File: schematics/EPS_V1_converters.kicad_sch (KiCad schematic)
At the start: 30 parts, among them U2 TPS62132RGTR, U3 TPS62133RGTR, U6 TPS61088RHLR

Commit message: Fix NC pins, add 2 test points & silkscreen labels
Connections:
- net GND: now also U2.4 (PG), U3.4 (PG), U6.11 (NC), U6.12 (NC)
- no-connect marks 5 -> 1
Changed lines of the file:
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@@
 	)
 	(junction
+		(at 135.89 166.37)
+		(diameter 0)
+		(color 0 0 0 0)
+	)
+	(junction
 		(at 137.16 134.62)
 		(diameter 0)
@@
 	)
 	(junction
+		(at 69.85 95.25)
+		(diameter 0)
+		(color 0 0 0 0)
+	)
+	(junction
 		(at 59.69 156.21)
 		(diameter 0)
@@
 	)
 	(junction
+		(at 134.62 127)
+		(diameter 0)
+		(color 0 0 0 0)
+	)
+	(junction
 		(at 114.3 54.61)
 		(diameter 0)
@@
 	)
 	(junction
-		(at 129.54 171.45)
+		(at 134.62 124.46)
 		(diameter 0)
 		(color 0 0 0 0)
 	)
 	(junction
-		(at 105.41 67.31)
+		(at 129.54 171.45)
 		(diameter 0)
 		(color 0 0 0 0)
 	)
 	(junction
-		(at 134.62 124.46)
+		(at 105.41 67.31)
 		(diameter 0)
 		(color 0 0 0 0)
@@
 	)
 	(junction
-		(at 135.89 163.83)
-		(diameter 0)
-		(color 0 0 0 0)
-	)
-	(junction
 		(at 114.3 57.15)
 		(diameter 0)
@@
 	)
 	(junction
+		(at 135.89 163.83)
+		(diameter 0)
+		(color 0 0 0 0)
+	)
+	(junction
 		(at 114.3 49.53)
 		(diameter 0)
@@
 		(at 69.85 85.09)
 	)
-	(no_connect
-		(at 129.54 166.37)
-	)
-	(no_connect
-		(at 69.85 95.25)
-	)
-	(no_connect
-		(at 129.54 127)
-	)
-	(no_connect
-		(at 69.85 92.71)
-	)
 	(wire
 		(pts
@@
 	(wire
 		(pts
+			(xy 135.89 166.37) (xy 135.89 163.83)
+		)
+		(stroke
+			(width 0)
+			(type default)
+		)
+	)
+	(wire
+		(pts
 			(xy 45.72 64.77) (xy 69.85 64.77)
 		)
@@
 	(wire
 		(pts
-			(xy 134.62 124.46) (xy 134.62 125.73)
+			(xy 134.62 124.46) (xy 134.62 127)
 		)
 		(stroke
@@
 	(wire
 		(pts
+			(xy 129.54 166.37) (xy 135.89 166.37)
+		)
+		(stroke
+			(width 0)
+			(type default)
+		)
+	)
+	(wire
+		(pts
 			(xy 45.72 156.21) (xy 59.69 156.21)
 		)
@@
 	(wire
 		(pts
+			(xy 69.85 92.71) (xy 69.85 95.25)
+		)
+		(stroke
+			(width 0)
+			(type default)
+		)
+	)
+	(wire
+		(pts
 			(xy 68.58 41.91) (xy 69.85 41.91)
 		)
@@
 	(wire
 		(pts
+			(xy 129.54 127) (xy 134.62 127)
+		)
+		(stroke
+			(width 0)
+			(type default)
+		)
+	)
+	(wire
+		(pts
 			(xy 105.41 29.21) (xy 114.3 29.21)
 		)
@@
 	(symbol
 		(lib_id "power:GND")
-		(at 135.89 163.83 0)
+		(at 135.89 166.37 0)
 		(unit 1)
 		(body_style 1)
@@
 		(dnp no)
 		(property "Reference" "#PWR017"
-			(at 135.89 170.18 0)
+			(at 135.89 172.72 0)
 			(hide yes)
 			(show_name no)
@@
 		)
 		(property "Value" "GND"
-			(at 135.89 167.894 0)
+			(at 135.89 170.434 0)
 			(show_name no)
 			(do_not_autoplace no)
@@
 		)
 		(property "Footprint" ""
-			(at 135.89 163.83 0)
+			(at 135.89 166.37 0)
 			(hide yes)
 			(show_name no)
@@
 		)
 		(property "Datasheet" ""
-			(at 135.89 163.83 0)
+			(at 135.89 166.37 0)
 			(hide yes)
 			(show_name no)
@@
 		)
 		(property "Description" "Power symbol creates a global label with name \"GND\" , ground"
-			(at 135.89 163.83 0)
+			(at 135.89 166.37 0)
 			(hide yes)
 			(show_name no)
@@
 	(symbol
 		(lib_id "power:GND")
-		(at 134.62 125.73 0)
+		(at 134.62 127 0)
 		(unit 1)
 		(body_style 1)
@@
 		(dnp no)
 		(property "Reference" "#PWR023"
-			(at 134.62 132.08 0)
+			(at 134.62 133.35 0)
 			(hide yes)
 			(show_name no)
@@
 		)
 		(property "Value" "GND"
-			(at 134.62 129.794 0)
+			(at 134.62 131.064 0)
 			(show_name no)
 			(do_not_autoplace no)
@@
 		)
 		(property "Footprint" ""
-			(at 134.62 125.73 0)
+			(at 134.62 127 0)
 			(hide yes)
 			(show_name no)
@@
 		)
 		(property "Datasheet" ""
-			(at 134.62 125.73 0)
+			(at 134.62 127 0)
 			(hide yes)
 			(show_name no)
@@
 		)
 		(property "Description" "Power symbol creates a global label with name \"GND\" , ground"
-			(at 134.62 125.73 0)
+			(at 134.62 127 0)
 			(hide yes)
 			(show_name no)
@@
 					(unit 1)
 				)
+			)
+		)
+	)
+	(symbol
+		(lib_id "power:GND")
+		(at 69.85 95.25 0)
+		(unit 1)
+		(body_style 1)
+		(exclude_from_sim no)
+		(in_bom yes)
+		(on_board yes)
+		(in_pos_files yes)
+		(dnp no)
+		(property "Reference" "#PWR081"
+			(at 69.85 101.6 0)
+			(hide yes)
+			(show_name no)
+			(do_not_autoplace no)
+			(effects
+				(font
+					(size 1.27 1.27)
+				)
+			)
+		)
+		(property "Value" "GND"
+			(at 69.85 99.314 0)
+			(show_name no)
+			(do_not_autoplace no)
+			(effects
+				(font
+					(size 1.27 1.27)
+				)
+			)
+		)
+		(property "Footprint" ""
+			(at 69.85 95.25 0)
+			(hide yes)
+			(show_name no)
+			(do_not_autoplace no)
+			(effects
+				(font
+					(size 1.27 1.27)
+				)
+			)
+		)
+		(property "Datasheet" ""
+			(at 69.85 95.25 0)
+			(hide yes)
+			(show_name no)
+			(do_not_autoplace no)
+			(effects
+				(font
+					(size 1.27 1.27)
+				)
+			)
+		)
+		(property "Description" "Power symbol creates a global label with name \"GND\" , ground"
+			(at 69.85 95.25 0)
+			(hide yes)
+			(show_name no)
+			(do_not_autoplace no)
+			(effects
+				(font
+					(size 1.27 1.27)
+				)
+			)
+		)
+		(pin "1"
+		)
+		(instances
+			(project "EPS_V1"
+				(path "/85157432-5d03-48fa-ab40-27ed3d133f47/d39b1cbe-de60-4da6-b23b-bfd89ef5271a"
+					(reference "#PWR081")
+					(unit 1)
+				)

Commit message: Fix silkscreen; Fix component value style
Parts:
- C2, C6, C_AVIN1, C_AVIN2: value 0.1u -> 100n
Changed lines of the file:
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@@
 			)
 		)
-		(property "Value" "0.1u"
+		(property "Value" "100n"
 			(at 42.926 133.35 0)
 			(show_name no)
@@
 			)
 		)
-		(property "Value" "0.1u"
+		(property "Value" "100n"
 			(at 108.204 39.37 0)
 			(show_name no)
@@
 			)
 		)
-		(property "Value" "0.1u"
+		(property "Value" "100n"
 			(at 49.276 44.45 0)
 			(show_name no)
@@
 			)
 		)
-		(property "Value" "0.1u"
+		(property "Value" "100n"
 			(at 42.926 172.72 0)
 			(show_name no)

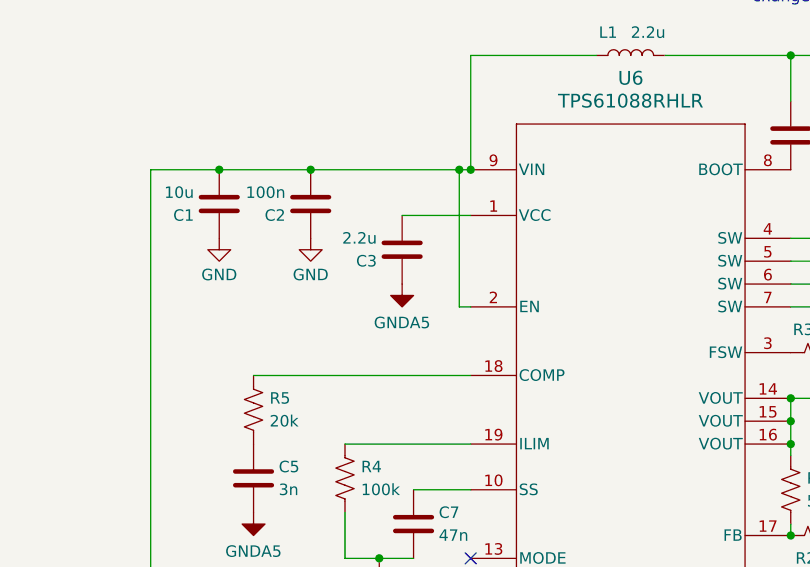
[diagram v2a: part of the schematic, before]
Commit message: fix U6 EN pin, add ALRT pullup R, update 3dmodels, regen step
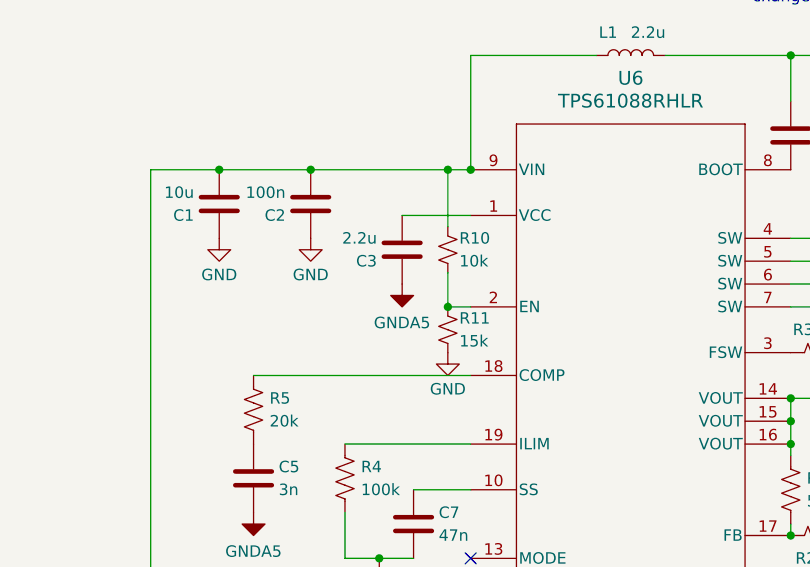
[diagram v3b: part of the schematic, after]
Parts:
- added R10: 10k, Resistor_SMD:R_0603_1608Metric, symbol Device:R_Small_US
- added R11: 15k, Resistor_SMD:R_0603_1608Metric, symbol Device:R_Small_US
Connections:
- net CHG_OUT: now also R10.1; no longer U6.2 (EN)
- net GND: now also R11.2
- new net: R10.2, R11.1, U6.2 (EN)
